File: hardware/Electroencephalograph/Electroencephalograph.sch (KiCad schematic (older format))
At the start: 0 parts

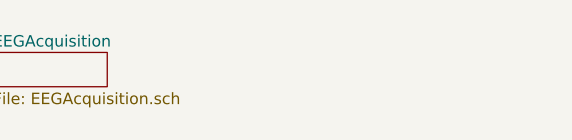
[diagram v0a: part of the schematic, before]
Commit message: paritial routing for analog part
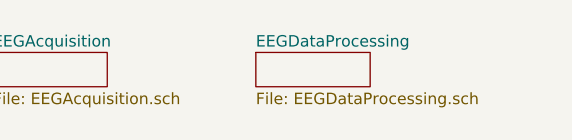
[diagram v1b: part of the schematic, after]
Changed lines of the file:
@@
 $Descr A4 11693 8268
 encoding utf-8
-Sheet 1 3
+Sheet 1 4
 Title ""
 Date ""
@@
 F1 "EEGAcquisition.sch" 50
 $EndSheet
+$Sheet
+S 4350 4400 500  150
+U 5E142744
+F0 "EEGDataProcessing" 50
+F1 "EEGDataProcessing.sch" 50
+$EndSheet
 $EndSCHEMATC

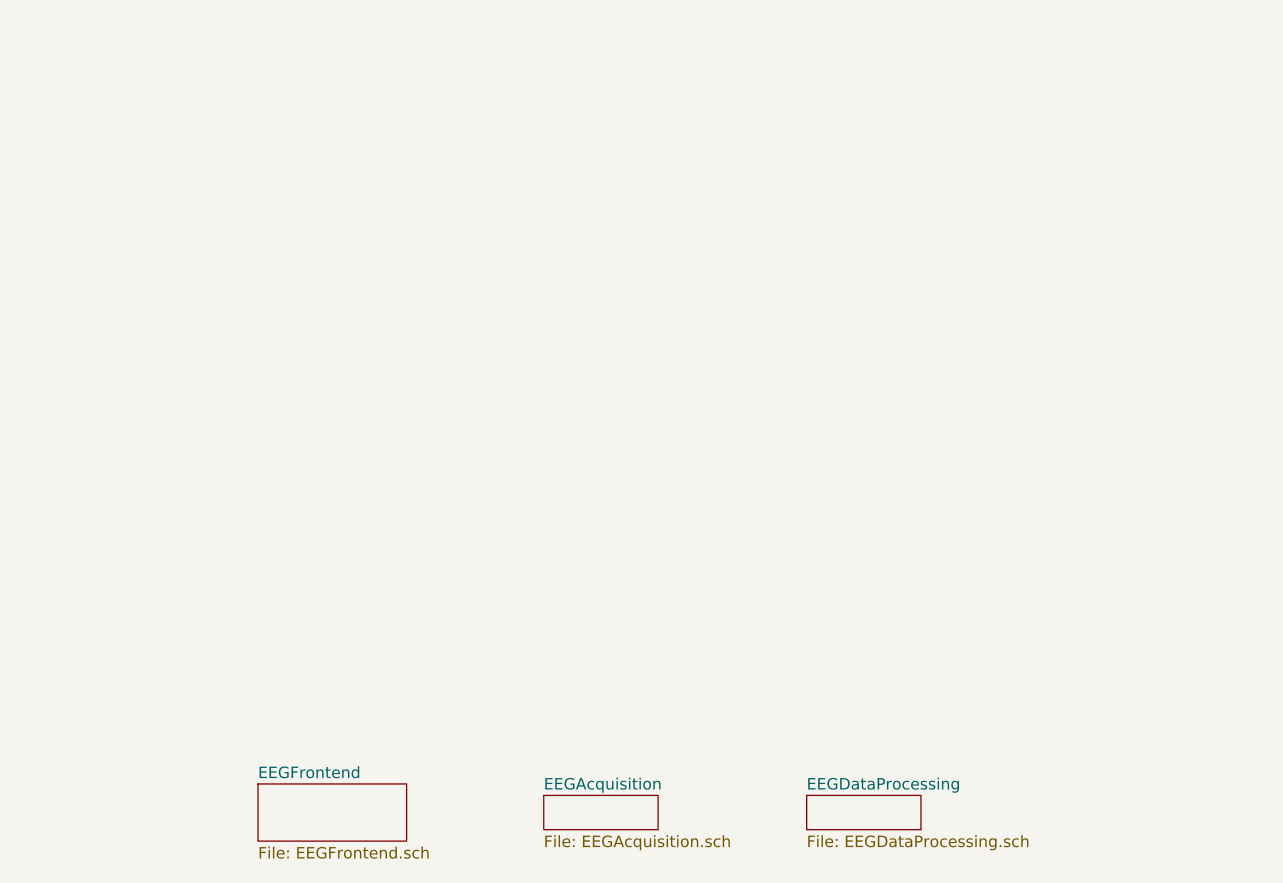
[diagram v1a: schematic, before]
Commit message: added spi isolator circuit
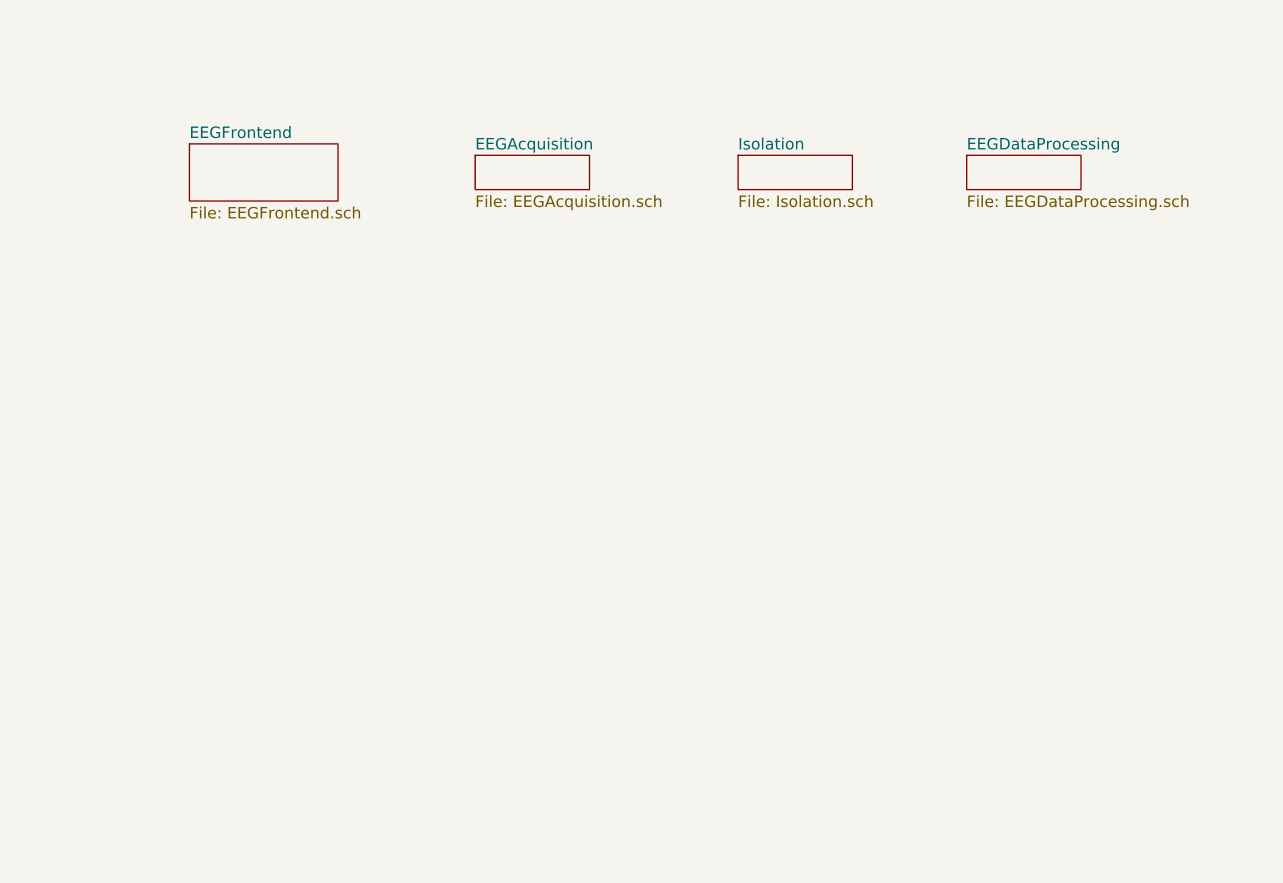
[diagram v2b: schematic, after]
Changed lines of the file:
@@
 $Descr A4 11693 8268
 encoding utf-8
-Sheet 1 4
+Sheet 1 5
 Title ""
 Date ""
@@
 $EndDescr
 $Sheet
-S 1950 4350 650  250
+S 1650 1550 650  250
 U 5DF4CFF8
 F0 "EEGFrontend" 50
@@
 $EndSheet
 $Sheet
-S 3200 4400 500  150
+S 2900 1600 500  150
 U 5DF61103
 F0 "EEGAcquisition" 50
@@
 $EndSheet
 $Sheet
-S 4350 4400 500  150
+S 5050 1600 500  150
 U 5E142744
 F0 "EEGDataProcessing" 50
 F1 "EEGDataProcessing.sch" 50
 $EndSheet
+$Sheet
+S 4050 1600 500  150
+U 5DFE0AD6
+F0 "Isolation" 50
+F1 "Isolation.sch" 50
+$EndSheet
 $EndSCHEMATC

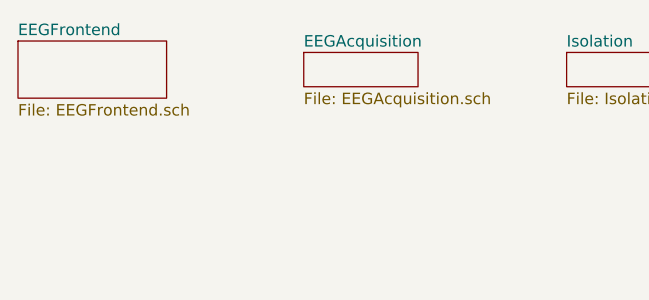
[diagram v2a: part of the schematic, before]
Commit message: power circuit supply added
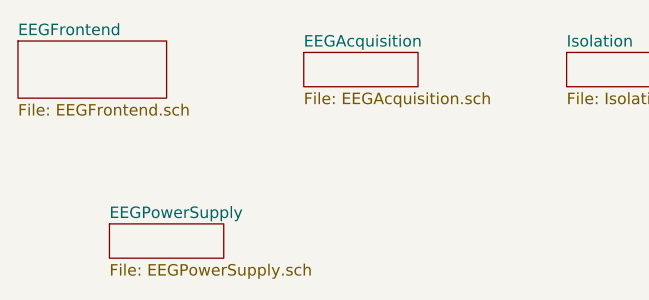
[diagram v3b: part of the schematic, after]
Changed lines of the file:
@@
 $Descr A4 11693 8268
 encoding utf-8
-Sheet 1 5
+Sheet 1 6
 Title ""
 Date ""
@@
 F1 "Isolation.sch" 50
 $EndSheet
+$Sheet
+S 2050 2350 500  150
+U 5E0992D6
+F0 "EEGPowerSupply" 50
+F1 "EEGPowerSupply.sch" 50
+$EndSheet
 $EndSCHEMATC

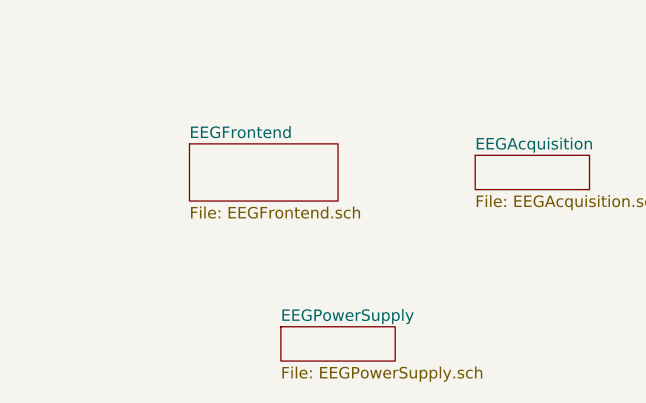
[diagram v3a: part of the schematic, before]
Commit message: enqable separate electrodes for each point
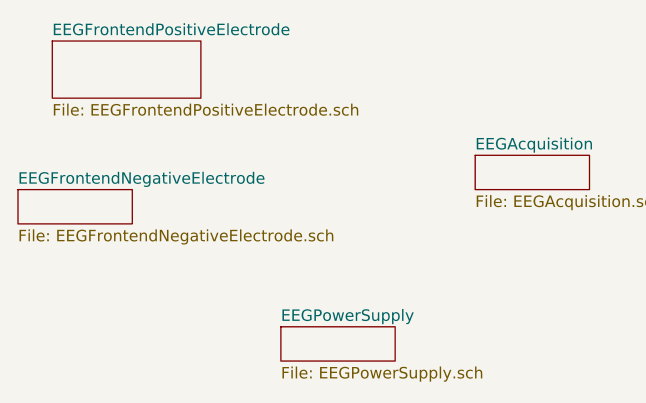
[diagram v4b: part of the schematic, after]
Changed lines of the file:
@@
 $Descr A4 11693 8268
 encoding utf-8
-Sheet 1 6
+Sheet 1 7
 Title ""
 Date ""
@@
 $EndDescr
 $Sheet
-S 1650 1550 650  250
+S 1050 1100 650  250
 U 5DF4CFF8
-F0 "EEGFrontend" 50
-F1 "EEGFrontend.sch" 50
+F0 "EEGFrontendPositiveElectrode" 50
+F1 "EEGFrontendPositiveElectrode.sch" 50
 $EndSheet
 $Sheet
@@
 F1 "EEGPowerSupply.sch" 50
 $EndSheet
+$Sheet
+S 900  1750 500  150
+U 5E312944
+F0 "EEGFrontendNegativeElectrode" 50
+F1 "EEGFrontendNegativeElectrode.sch" 50
+$EndSheet
 $EndSCHEMATC

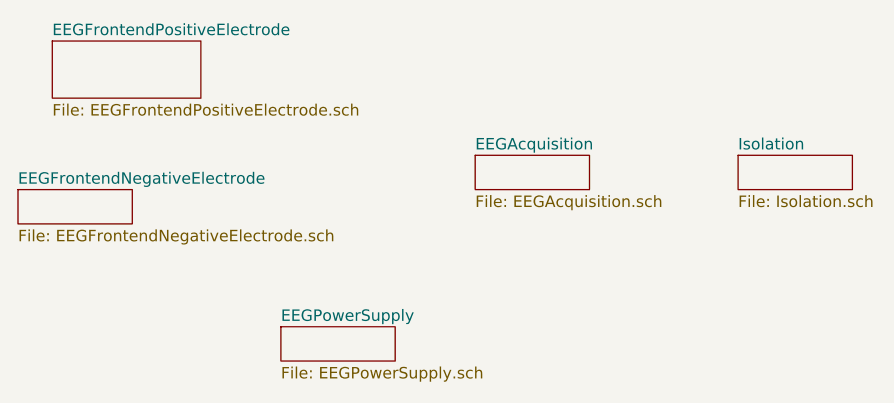
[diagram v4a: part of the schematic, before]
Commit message: removed external clk and vref
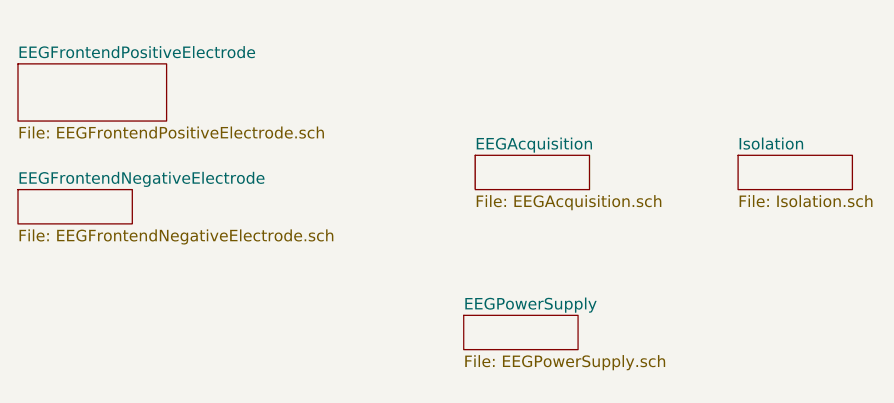
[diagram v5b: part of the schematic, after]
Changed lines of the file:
@@
 $EndDescr
 $Sheet
-S 1050 1100 650  250
+S 900  1200 650  250
 U 5DF4CFF8
 F0 "EEGFrontendPositiveElectrode" 50
@@
 $EndSheet
 $Sheet
-S 2050 2350 500  150
+S 2850 2300 500  150
 U 5E0992D6
 F0 "EEGPowerSupply" 50

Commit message: draft of PCB routing
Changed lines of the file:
@@
 S 900  1200 650  250
 U 5DF4CFF8
-F0 "EEGFrontendPositiveElectrode" 50
-F1 "EEGFrontendPositiveElectrode.sch" 50
+F0 "EEGFrontendElectrode1To4" 50
+F1 "EEGFrontendElectrode1To4.sch" 50
 $EndSheet
 $Sheet
@@
 S 900  1750 500  150
 U 5E312944
-F0 "EEGFrontendNegativeElectrode" 50
-F1 "EEGFrontendNegativeElectrode.sch" 50
+F0 "EEGFrontendElectrode5To8" 50
+F1 "EEGFrontendElectrode5To8.sch" 50
 $EndSheet
 $EndSCHEMATC

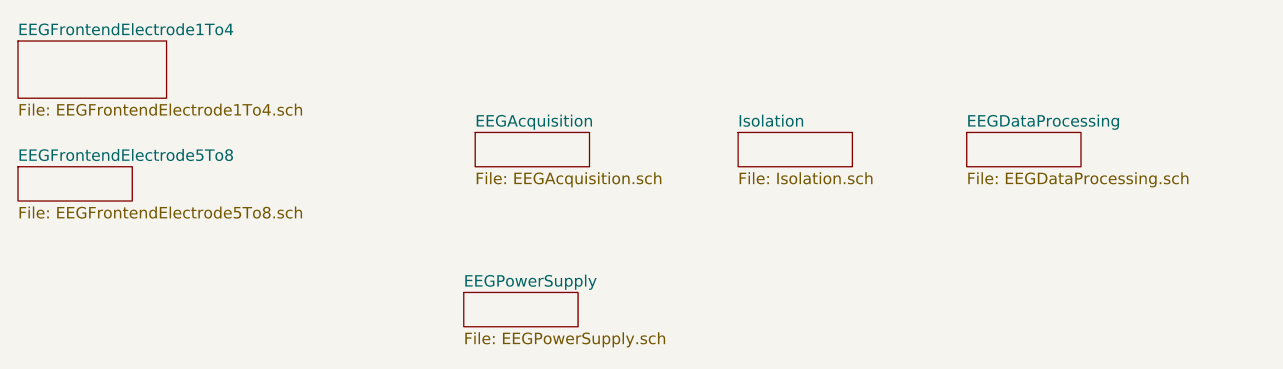
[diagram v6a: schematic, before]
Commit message: placing components groups
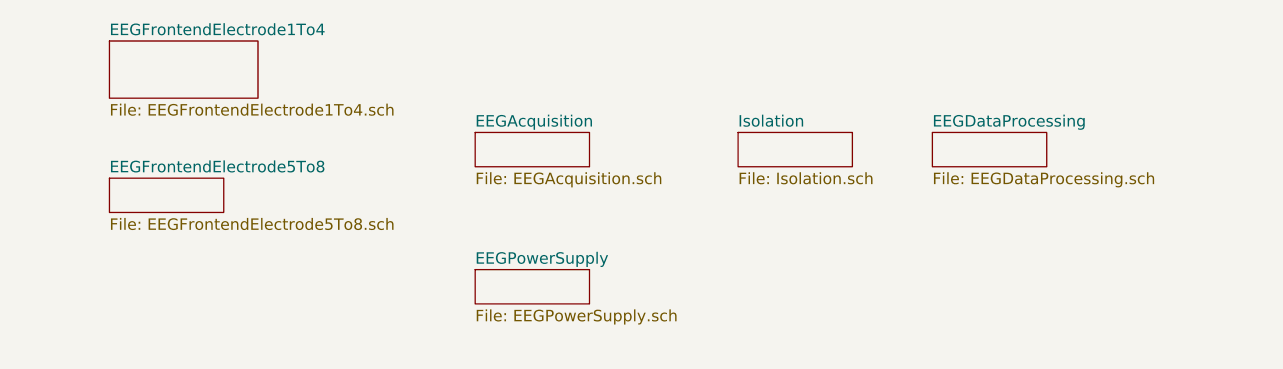
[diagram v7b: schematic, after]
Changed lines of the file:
@@
 $EndDescr
 $Sheet
-S 900  1200 650  250
+S 1300 1200 650  250
 U 5DF4CFF8
 F0 "EEGFrontendElectrode1To4" 50
@@
 $EndSheet
 $Sheet
-S 5050 1600 500  150
+S 4900 1600 500  150
 U 5E142744
 F0 "EEGDataProcessing" 50
@@
 $EndSheet
 $Sheet
-S 2850 2300 500  150
+S 2900 2200 500  150
 U 5E0992D6
 F0 "EEGPowerSupply" 50
@@
 $EndSheet
 $Sheet
-S 900  1750 500  150
+S 1300 1800 500  150
 U 5E312944
 F0 "EEGFrontendElectrode5To8" 50

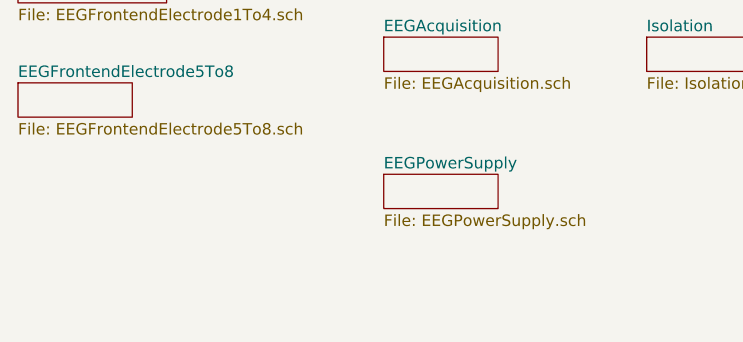
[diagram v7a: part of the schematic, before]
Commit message: route of analog part, update of 3d render
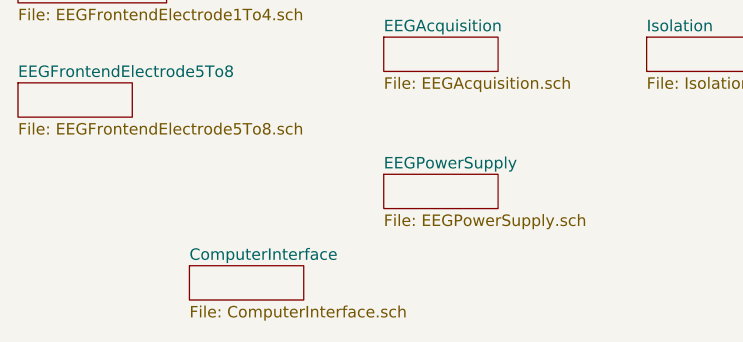
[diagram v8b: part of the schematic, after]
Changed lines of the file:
@@
 $Descr A4 11693 8268
 encoding utf-8
-Sheet 1 7
+Sheet 1 8
 Title ""
 Date ""
@@
 F1 "EEGFrontendElectrode5To8.sch" 50
 $EndSheet
+$Sheet
+S 2050 2600 500  150
+U 5E27E78E
+F0 "ComputerInterface" 50
+F1 "ComputerInterface.sch" 50
+$EndSheet
 $EndSCHEMATC
